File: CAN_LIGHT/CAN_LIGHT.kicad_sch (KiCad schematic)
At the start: 2 parts, among them U1 TCAN334, U2 SN74LVC1T45DCK

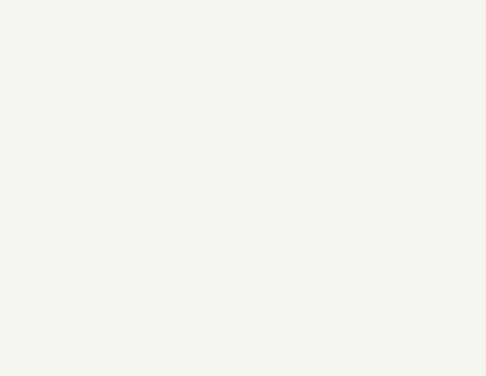
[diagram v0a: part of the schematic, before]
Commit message: Add custom WRGB symbol
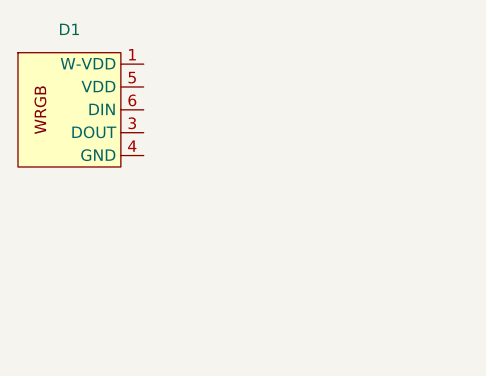
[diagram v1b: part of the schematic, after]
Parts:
- added D1: ~, symbol LED:IN-PI4818QAS5R5G5BPW
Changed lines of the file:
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@@
+    )
+  )
+  (symbol (lib_id "LED:IN-PI4818QAS5R5G5BPW") (at 29.21 30.48 0) (unit 1)
+    (in_bom yes) (on_board yes) (dnp no) (fields_autoplaced)
+    (property "Reference" "D1" (at 34.925 15.24 0)
+      (effects (font (size 1.27 1.27)))
+    )
+    (property "Value" "~" (at 30.48 20.32 0)
+      (effects (font (size 1.27 1.27)))
+    )
+    (property "Footprint" "" (at 30.48 20.32 0)
+      (effects (font (size 1.27 1.27)) hide)
+    )
+    (property "Datasheet" "" (at 30.48 20.32 0)
+      (effects (font (size 1.27 1.27)) hide)
+    )
+    (pin "1")
+    (pin "2")
+    (pin "3")
+    (pin "4")
+    (pin "5")
+    (pin "6")
+    (instances
+      (project "CAN_LIGHT"
+        (path "/d4f25219-6cef-4e47-aded-6c41d03d24e2"
+          (reference "D1") (unit 1)
+        )
+      )
     )
   )

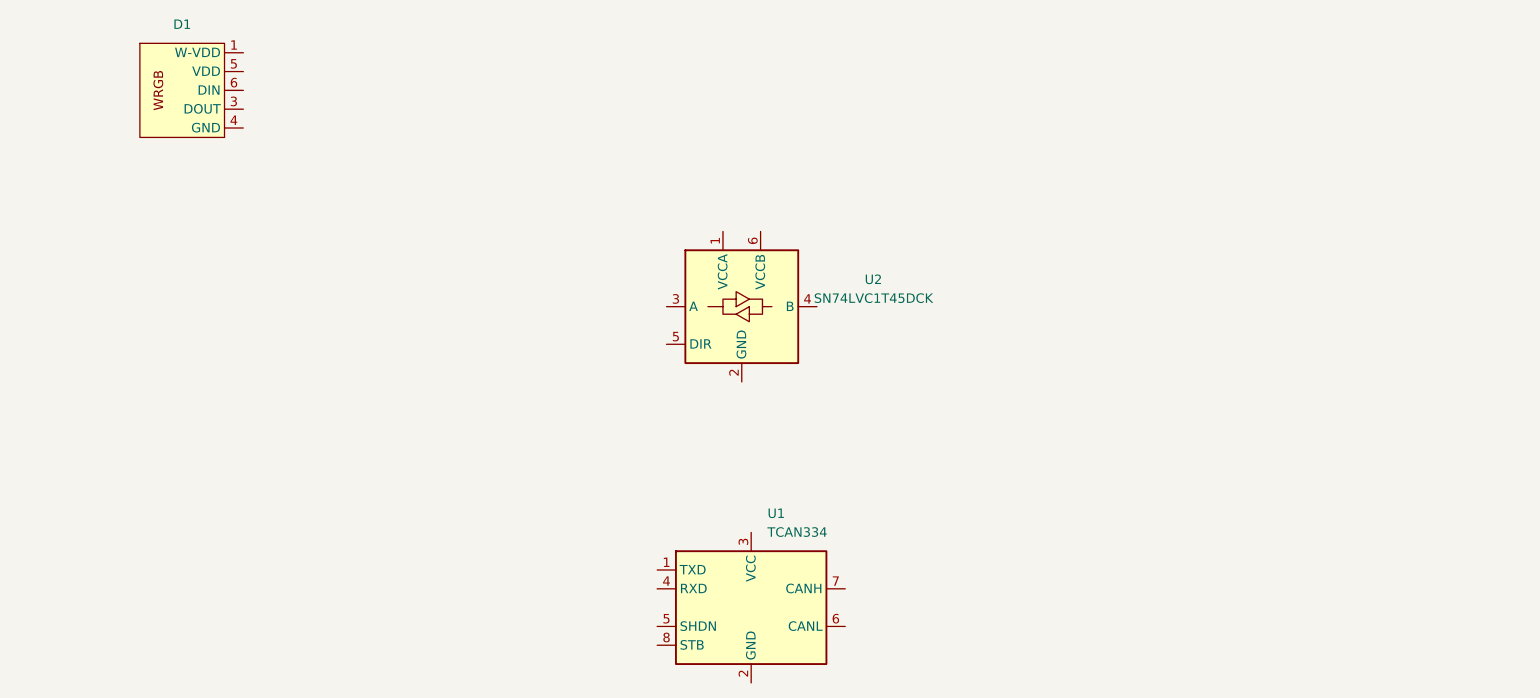
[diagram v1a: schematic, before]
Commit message: Select and implement MCU; Add TagConnect port
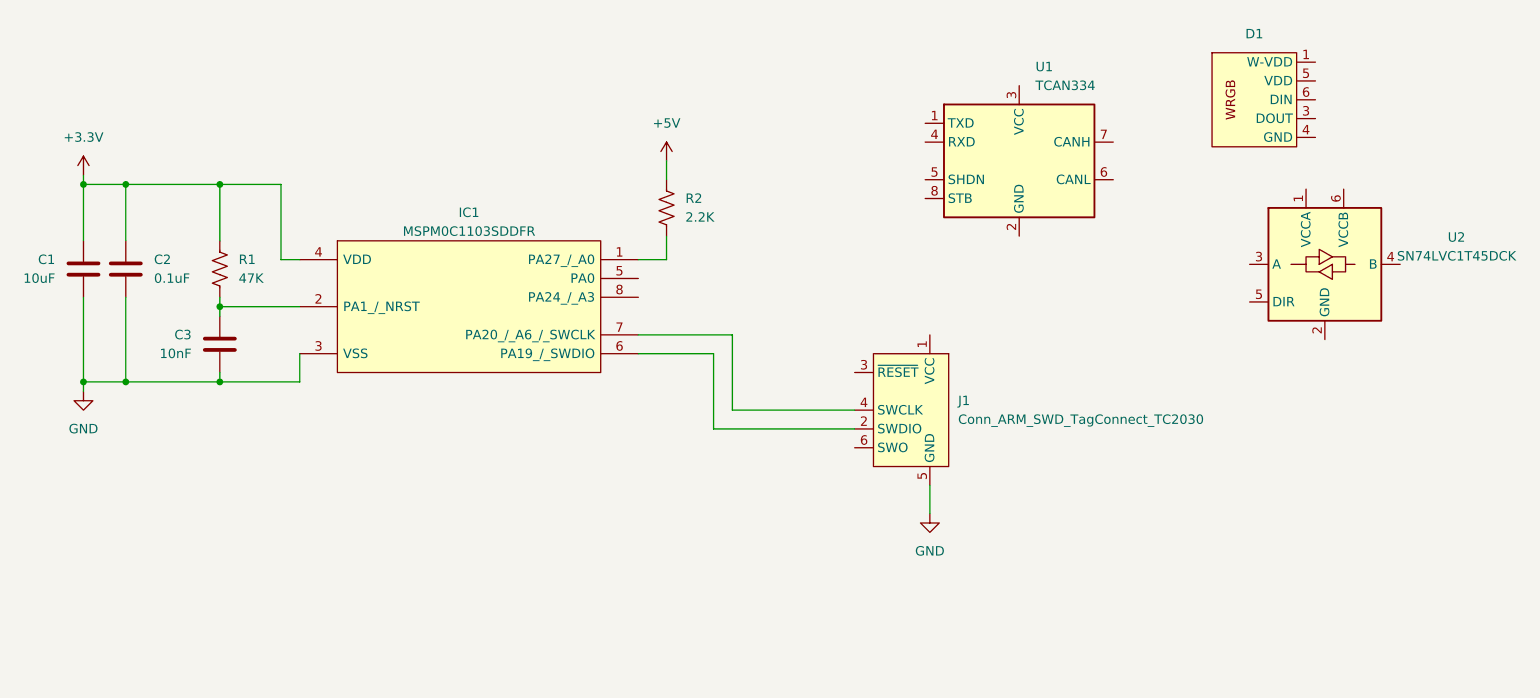
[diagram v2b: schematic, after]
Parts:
- added C1: 10uF, Capacitor_SMD:C_0603_1608Metric_Pad1.08x0.95mm_HandSolder, symbol Device:C
- added C2: 0.1uF, Capacitor_SMD:C_0603_1608Metric_Pad1.08x0.95mm_HandSolder, symbol Device:C
- added C3: 10nF, Capacitor_SMD:C_0603_1608Metric_Pad1.08x0.95mm_HandSolder, symbol Device:C
- added IC1: MSPM0C1103SDDFR, SOT65P280X110-8N, symbol MSPM0C1103SDDFR:MSPM0C1103SDDFR
- added J1: Conn_ARM_SWD_TagConnect_TC2030, Connector:Tag-Connect_TC2030-IDC-FP_2x03_P1.27mm_Vertical, symbol Connector:Conn_ARM_SWD_TagConnect_TC2030
- added R1: 47K, Resistor_SMD:R_0603_1608Metric_Pad0.98x0.95mm_HandSolder, symbol Device:R_US
- added R2: 2.2K, Resistor_SMD:R_0603_1608Metric_Pad0.98x0.95mm_HandSolder, symbol Device:R_US
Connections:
- new net: IC1.1 (PA27_/_A0), R2.2
- new net: C3.1, IC1.2 (PA1_/_NRST), R1.2
- new net: IC1.6 (PA19_/_SWDIO), J1.2 (SWDIO)
- new net: IC1.7 (PA20_/_A6_/_SWCLK), J1.4 (SWCLK)
- new net +3.3V: C1.1, C2.1, IC1.4 (VDD), R1.1
- new net +5V: R2.1
- new net GND: C1.2, C2.2, C3.2, IC1.3 (VSS), J1.5 (GND)
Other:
- moved on the sheet: D1, U1, U2

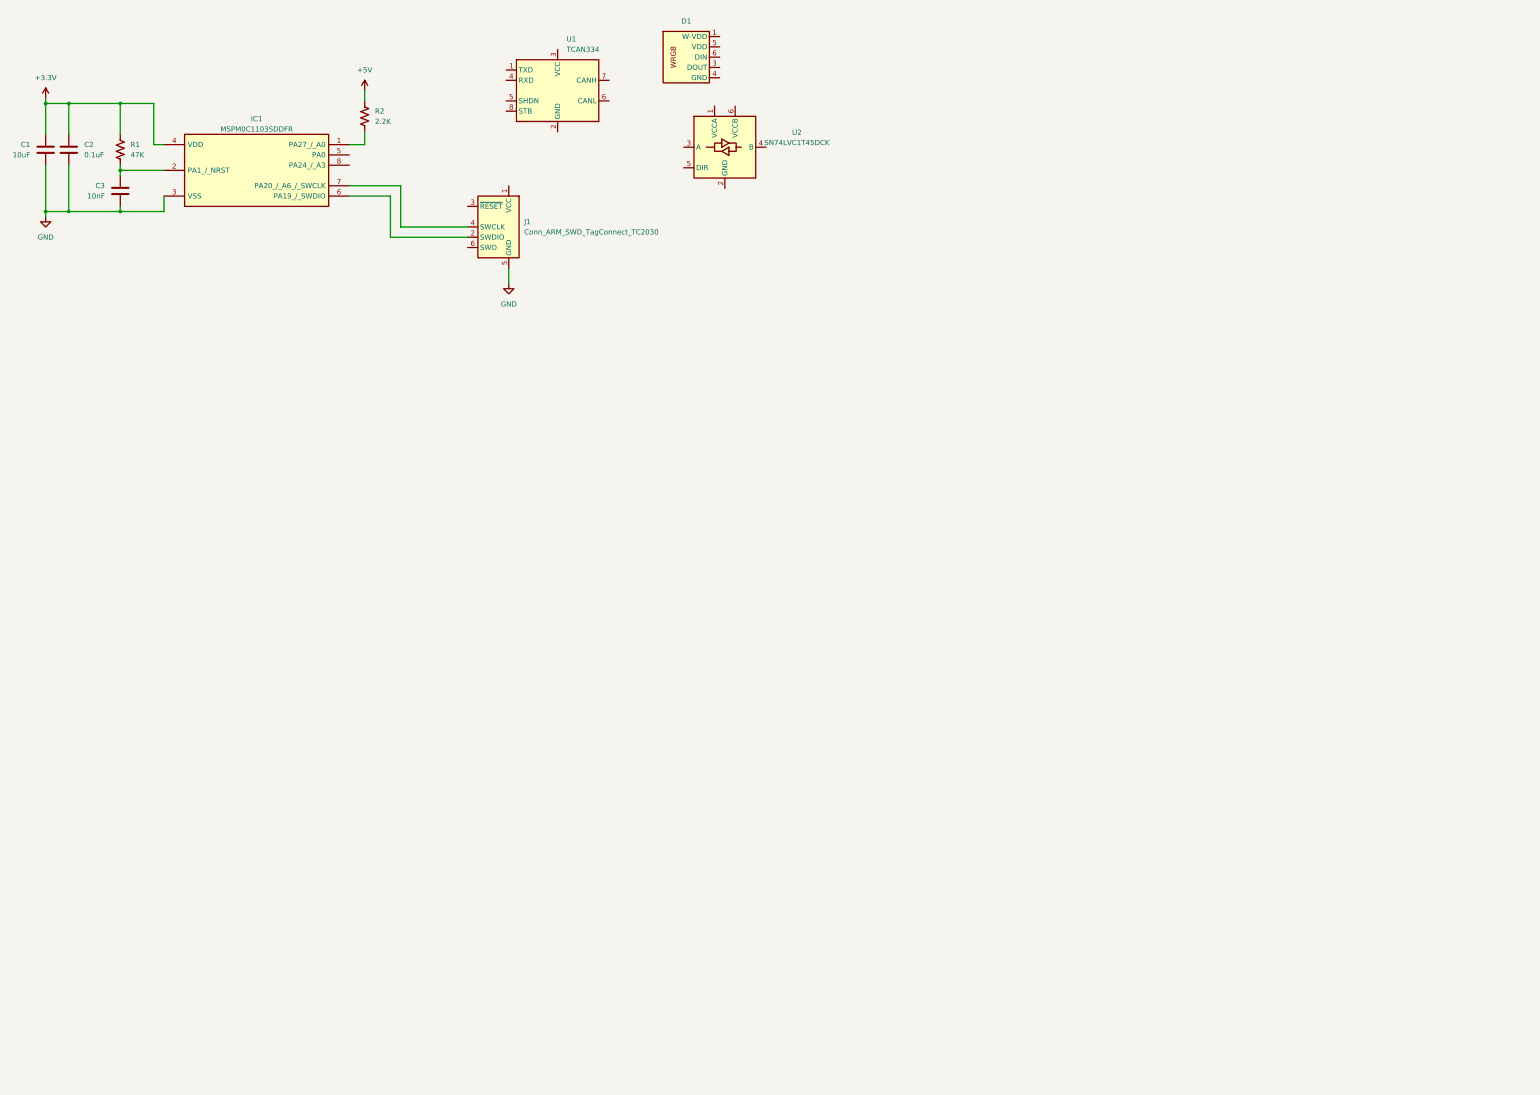
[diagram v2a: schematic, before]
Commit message: Wire up LEDs, MCU, CAN transceiver, and input port
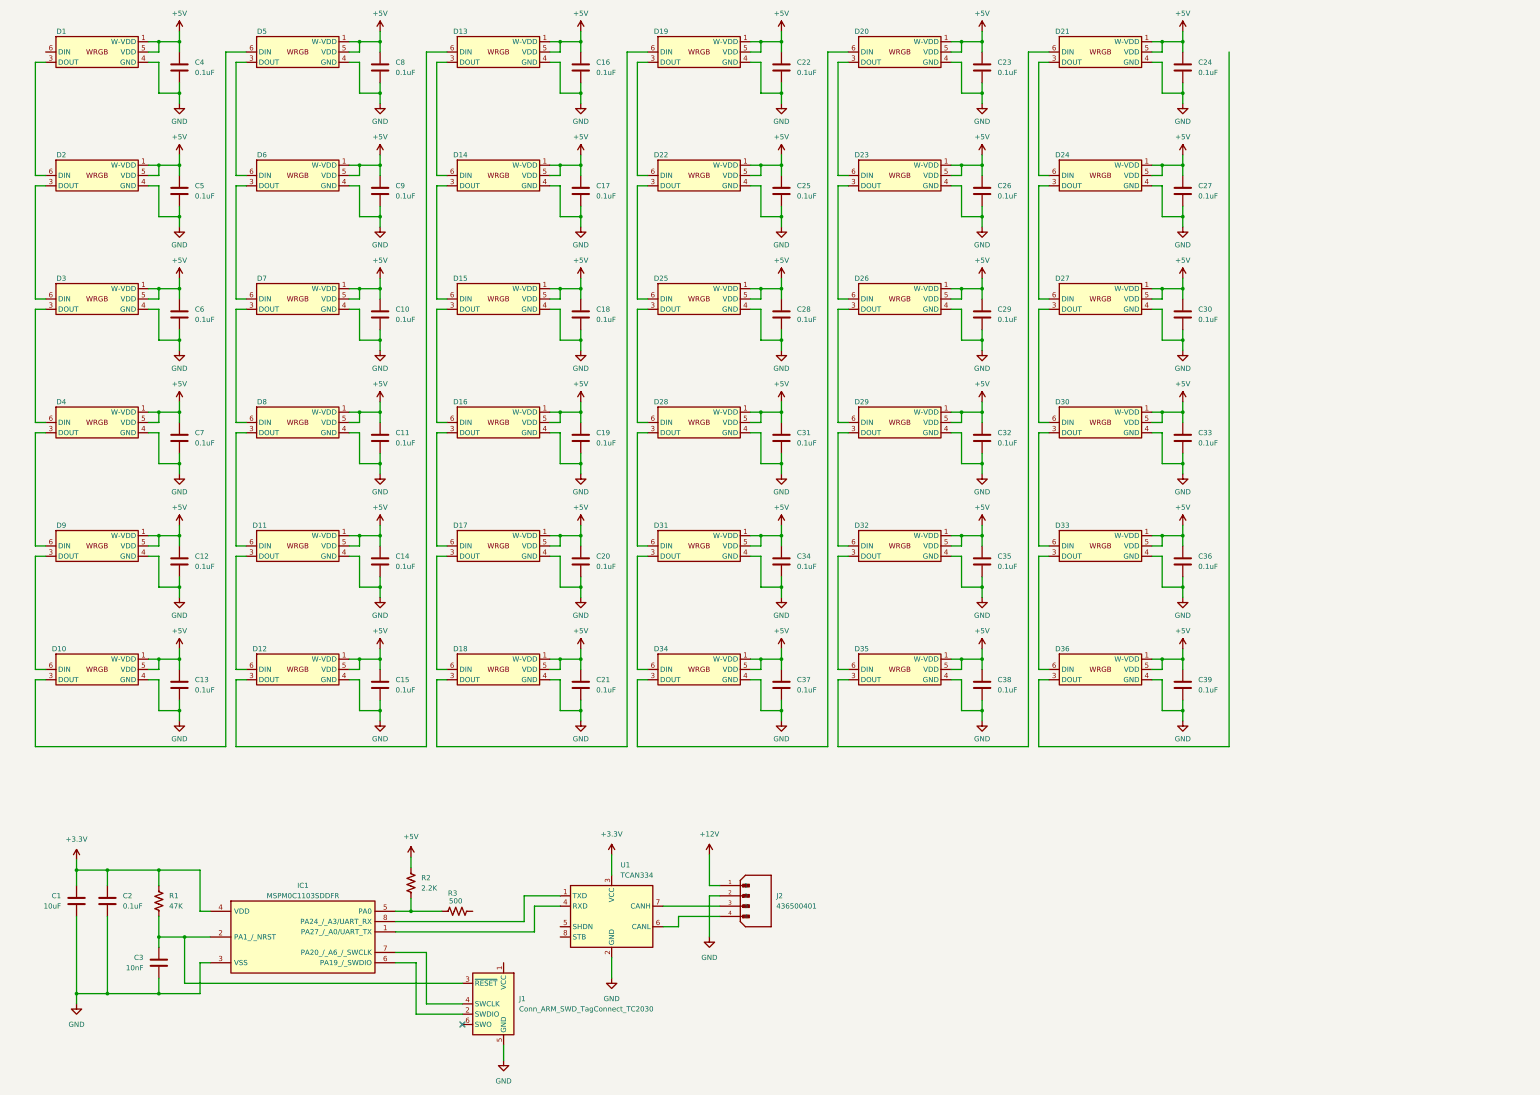
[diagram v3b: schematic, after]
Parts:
- removed U2: SN74LVC1T45DCK, Package_TO_SOT_SMD:SOT-363_SC-70-6, symbol Logic_LevelTranslator:SN74LVC1T45DCK
- added C10, C11, C12, C13, C14, C15, C16, C17, C18, C19, C20, C21, C22, C23, C24, C25, C26, C27, C28, C29, C30, C31, C32, C33, C34, C35, C36, C37, C38, C39, C4, C5, C6, C7, C8, C9: 0.1uF, Capacitor_SMD:C_0603_1608Metric_Pad1.08x0.95mm_HandSolder, symbol Device:C
- added D10, D11, D12, D13, D14, D15, D16, D17, D18, D19, D2, D20, D21, D22, D23, D24, D25, D26, D27, D28, D29, D3, D30, D31, D32, D33, D34, D35, D36, D4, D5, D6, D7, D8, D9: ~, symbol LED:IN-PI4818QAS5R5G5BPW
- added J2: 436500401, 436500401:MOLEX_436500401, symbol 0436500401:436500401
- added R3: 500, Resistor_SMD:R_0603_1608Metric_Pad0.98x0.95mm_HandSolder, symbol Device:R_US
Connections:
- net +3.3V: now also U1.3 (VCC)
- net +5V: now also D1.1 (W-VDD), D1.5 (VDD), C10.1, C11.1, C12.1, C13.1, C14.1, C15.1, C16.1, C17.1, C18.1, C19.1, C20.1, C21.1, C22.1, C23.1, C24.1, C25.1, C26.1, C27.1, C28.1, C29.1, C30.1, C31.1, C32.1, C33.1, C34.1, C35.1, C36.1, C37.1, C38.1, C39.1, C4.1, C5.1, C6.1, C7.1, C8.1, C9.1, D10.1 (W-VDD), D10.5 (VDD), D11.1 (W-VDD), D11.5 (VDD), D12.1 (W-VDD), D12.5 (VDD), D13.1 (W-VDD), D13.5 (VDD), D14.1 (W-VDD), D14.5 (VDD), D15.1 (W-VDD), D15.5 (VDD), D16.1 (W-VDD), D16.5 (VDD), D17.1 (W-VDD), D17.5 (VDD), D18.1 (W-VDD), D18.5 (VDD), D19.1 (W-VDD), D19.5 (VDD), D2.1 (W-VDD), D2.5 (VDD), D20.1 (W-VDD), D20.5 (VDD), D21.1 (W-VDD), D21.5 (VDD), D22.1 (W-VDD), D22.5 (VDD), D23.1 (W-VDD), D23.5 (VDD), D24.1 (W-VDD), D24.5 (VDD), D25.1 (W-VDD), D25.5 (VDD), D26.1 (W-VDD), D26.5 (VDD), D27.1 (W-VDD), D27.5 (VDD), D28.1 (W-VDD), D28.5 (VDD), D29.1 (W-VDD), D29.5 (VDD), D3.1 (W-VDD), D3.5 (VDD), D30.1 (W-VDD), D30.5 (VDD), D31.1 (W-VDD), D31.5 (VDD), D32.1 (W-VDD), D32.5 (VDD), D33.1 (W-VDD), D33.5 (VDD), D34.1 (W-VDD), D34.5 (VDD), D35.1 (W-VDD), D35.5 (VDD), D36.1 (W-VDD), D36.5 (VDD), D4.1 (W-VDD), D4.5 (VDD), D5.1 (W-VDD), D5.5 (VDD), D6.1 (W-VDD), D6.5 (VDD), D7.1 (W-VDD), D7.5 (VDD), D8.1 (W-VDD), D8.5 (VDD), D9.1 (W-VDD), D9.5 (VDD)
- net GND: now also D1.4 (GND), U1.2 (GND), C10.2, C11.2, C12.2, C13.2, C14.2, C15.2, C16.2, C17.2, C18.2, C19.2, C20.2, C21.2, C22.2, C23.2, C24.2, C25.2, C26.2, C27.2, C28.2, C29.2, C30.2, C31.2, C32.2, C33.2, C34.2, C35.2, C36.2, C37.2, C38.2, C39.2, C4.2, C5.2, C6.2, C7.2, C8.2, C9.2, D10.4 (GND), D11.4 (GND), D12.4 (GND), D13.4 (GND), D14.4 (GND), D15.4 (GND), D16.4 (GND), D17.4 (GND), D18.4 (GND), D19.4 (GND), D2.4 (GND), D20.4 (GND), D21.4 (GND), D22.4 (GND), D23.4 (GND), D24.4 (GND), D25.4 (GND), D26.4 (GND), D27.4 (GND), D28.4 (GND), D29.4 (GND), D3.4 (GND), D30.4 (GND), D31.4 (GND), D32.4 (GND), D33.4 (GND), D34.4 (GND), D35.4 (GND), D36.4 (GND), D4.4 (GND), D5.4 (GND), D6.4 (GND), D7.4 (GND), D8.4 (GND), D9.4 (GND), J2.2
- net at IC1.1 (PA27_/_A0/UART_TX): now also U1.4 (RXD); no longer R2.2
- net at C3.1, IC1.2 (PA1_/_NRST), R1.2: now also J1.3 (~{RESET})
- net at IC1.5 (PA0): now also R2.2, R3.1
- net at IC1.8 (PA24_/_A3/UART_RX): now also U1.1 (TXD)
- net at D1.3 (DOUT): now also D2.6 (DIN)
- net at U1.6 (CANL): now also J2.4
- net at U1.7 (CANH): now also J2.3
- new net: D11.3 (DOUT), D12.6 (DIN)
- new net: D11.6 (DIN), D8.3 (DOUT)
- new net: D10.6 (DIN), D9.3 (DOUT)
- new net: D4.3 (DOUT), D9.6 (DIN)
- new net: D33.3 (DOUT), D36.6 (DIN)
- new net: D30.3 (DOUT), D33.6 (DIN)
- new net: D14.3 (DOUT), D15.6 (DIN)
- new net: D13.3 (DOUT), D14.6 (DIN)
- new net: D12.3 (DOUT), D13.6 (DIN)
- new net: D3.3 (DOUT), D4.6 (DIN)
- new net: D20.6 (DIN), D34.3 (DOUT)
- new net: D31.3 (DOUT), D34.6 (DIN)
- new net: D27.3 (DOUT), D30.6 (DIN)
- new net: D24.3 (DOUT), D27.6 (DIN)
- new net: D15.3 (DOUT), D16.6 (DIN)
- new net: D21.3 (DOUT), D24.6 (DIN)
- new net: D21.6 (DIN), D35.3 (DOUT)
- new net: D10.3 (DOUT), D5.6 (DIN)
- new net: D17.3 (DOUT), D18.6 (DIN)
- new net: D16.3 (DOUT), D17.6 (DIN)
- new net: D20.3 (DOUT), D23.6 (DIN)
- new net: D5.3 (DOUT), D6.6 (DIN)
- new net: D25.3 (DOUT), D28.6 (DIN)
- new net: D22.3 (DOUT), D25.6 (DIN)
- new net: D2.3 (DOUT), D3.6 (DIN)
- new net: D28.3 (DOUT), D31.6 (DIN)
- new net: D26.3 (DOUT), D29.6 (DIN)
- new net: D23.3 (DOUT), D26.6 (DIN)
- new net: D19.3 (DOUT), D22.6 (DIN)
- new net: D18.3 (DOUT), D19.6 (DIN)
- new net: D7.3 (DOUT), D8.6 (DIN)
- new net: D6.3 (DOUT), D7.6 (DIN)
- new net: D32.3 (DOUT), D35.6 (DIN)
- new net: D29.3 (DOUT), D32.6 (DIN)
- new net +12V: J2.1
- no-connect marks 0 -> 1
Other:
- moved on the sheet: C1, C2, C3, IC1, J1, R1, R2, U1

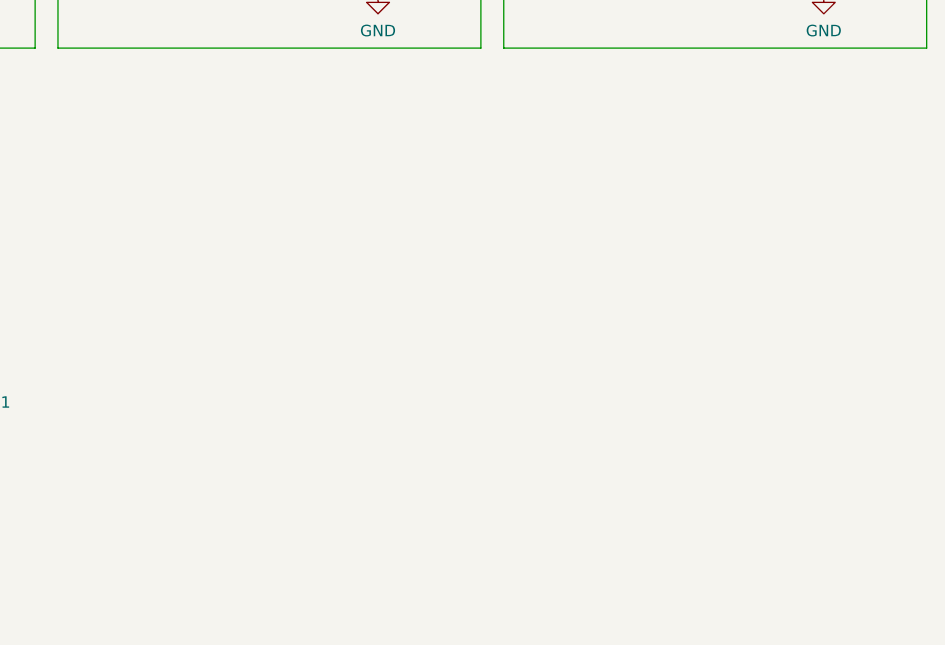
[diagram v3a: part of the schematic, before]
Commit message: Add 5V to 3V3 LDO
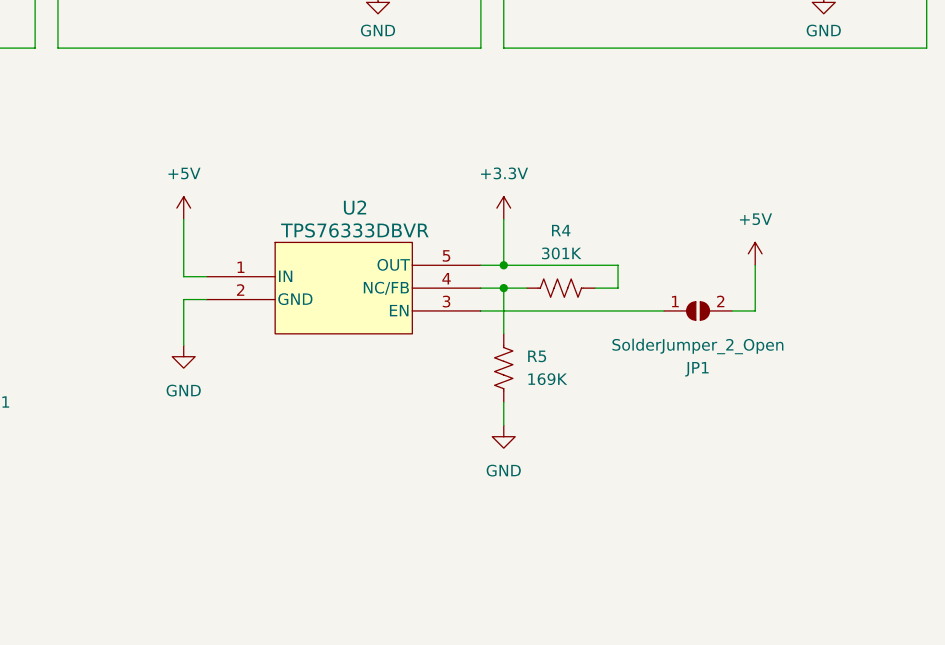
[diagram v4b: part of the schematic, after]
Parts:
- added JP1: SolderJumper_2_Open, symbol Jumper:SolderJumper_2_Open
- added R4: 301K, Resistor_SMD:R_0603_1608Metric_Pad0.98x0.95mm_HandSolder, symbol Device:R_US
- added R5: 169K, Resistor_SMD:R_0603_1608Metric_Pad0.98x0.95mm_HandSolder, symbol Device:R_US
- added U2: TPS76333DBVR, DBV5, symbol TPS76333DBVR:TPS76333DBVR
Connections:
- net +3.3V: now also R4.2, U2.5 (OUT)
- net +5V: now also JP1.2 (B), U2.1 (IN)
- net GND: now also R5.2, U2.2 (GND)
- new net: R4.1, R5.1, U2.4 (NC/FB)
- new net: JP1.1 (A), U2.3 (EN)
